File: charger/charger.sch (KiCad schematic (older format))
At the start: 43 parts, among them J1 Barrel_Jack, P1 Digital, P10 CONN_01X01, P11 CONN_01X01, P12 CONN_01X01, P13 CONN_01X01, P2 Power, P3 Analog, P4 Analog, P5 PWM, P6 PWM, P7 Communication, P8 CONN_01X01, P9 CONN_01X01, Q16 2SC1815, Q17 NDP6020, Q18 2SC1815, Q19 NDP6020, Q2 2SC1815, Q20 2SC1815, Q21 NDP6020, Q4 NDP6020, Q5 NDP6020, Q6 NDP6020, Q7 NDP6020, Q8 NDP6020, U1 tp4056charger, U2 tp4056charger, U3 tp4056charger, U4 tp4056charger

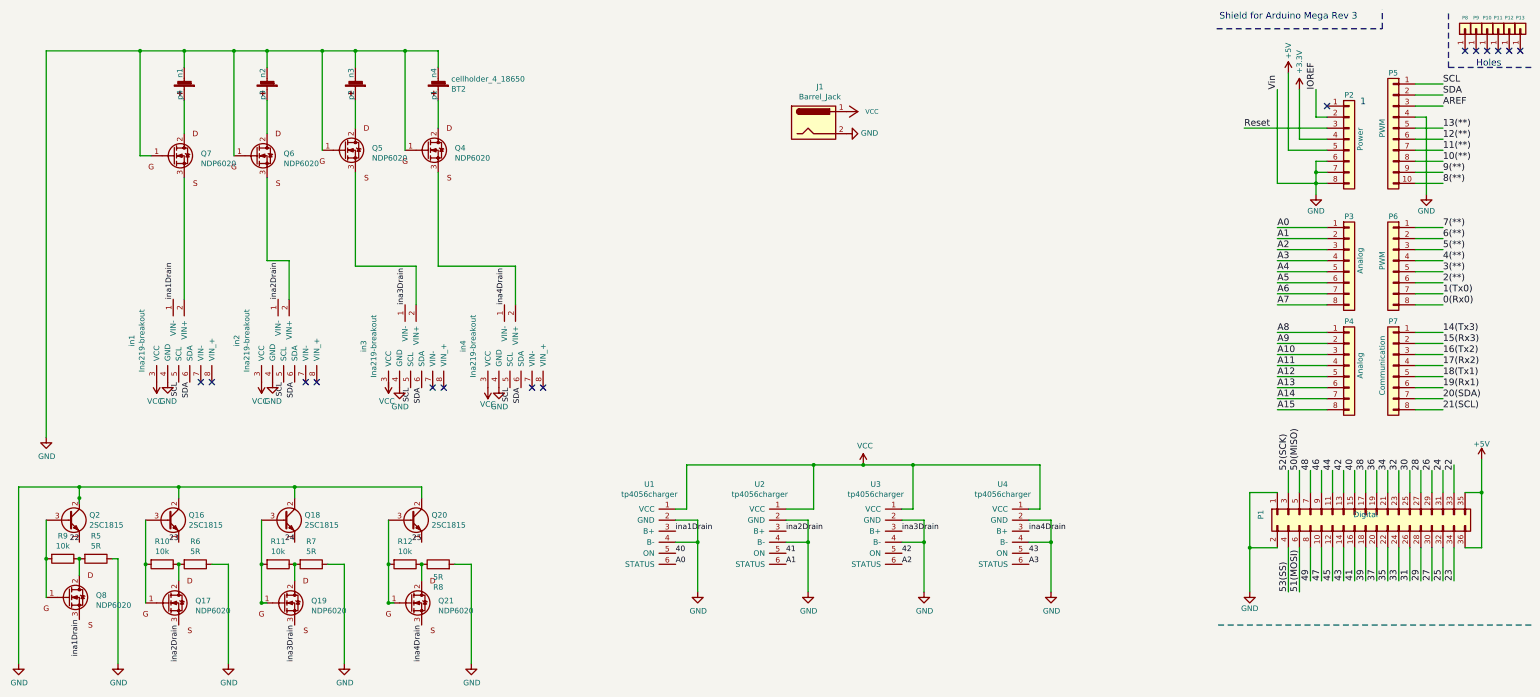
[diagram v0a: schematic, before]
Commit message: adding 2 layer layout, circuit design for 1 and 2 layer
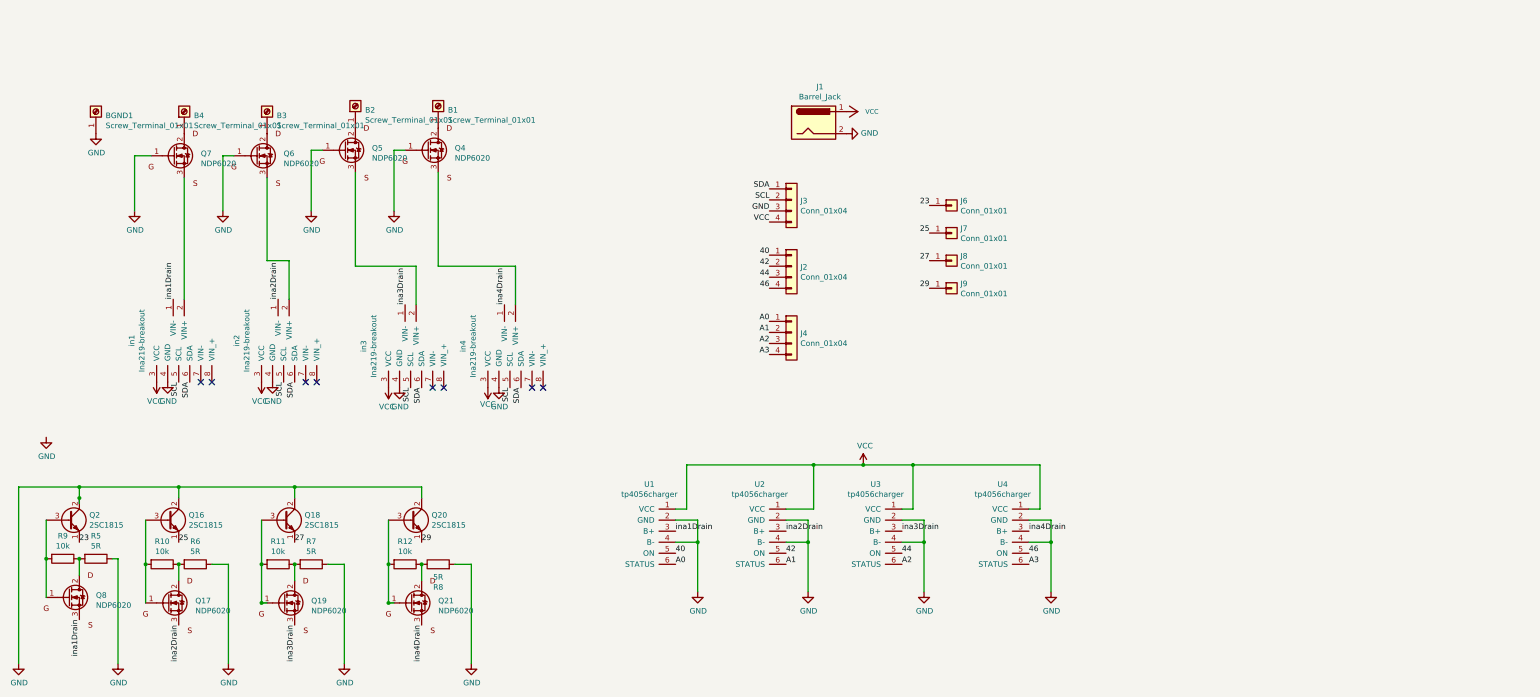
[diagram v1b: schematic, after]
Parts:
- removed BT2: cellholder_4_18650, charger:battery_holder, symbol charger-rescue:cellholder_4_18650-batteryholder1
- removed P1: Digital, Socket_Arduino_Mega:Socket_Strip_Arduino_2x18, symbol Connector_Generic:Conn_02x18_Odd_Even
- removed P10, P11, P12, P13, P8, P9: CONN_01X01, Socket_Arduino_Mega:Arduino_1pin, symbol Connector_Generic:Conn_01x01
- removed P2: Power, Socket_Arduino_Mega:Socket_Strip_Arduino_1x08, symbol Connector_Generic:Conn_01x08
- removed P3, P4: Analog, Socket_Arduino_Mega:Socket_Strip_Arduino_1x08, symbol Connector_Generic:Conn_01x08
- removed P5: PWM, Socket_Arduino_Mega:Socket_Strip_Arduino_1x10, symbol Connector_Generic:Conn_01x10
- removed P6: PWM, Socket_Arduino_Mega:Socket_Strip_Arduino_1x08, symbol Connector_Generic:Conn_01x08
- removed P7: Communication, Socket_Arduino_Mega:Socket_Strip_Arduino_1x08, symbol Connector_Generic:Conn_01x08
- added B1, B2, B3, B4, BGND1: Screw_Terminal_01x01, MountingHole:MountingHole_2.2mm_M2_DIN965_Pad, symbol Connector:Screw_Terminal_01x01
- added J2, J3, J4: Conn_01x04, Connector_PinHeader_2.54mm:PinHeader_1x04_P2.54mm_Vertical, symbol Connector_Generic:Conn_01x04
- added J6, J7, J8, J9: Conn_01x01, Connector_PinHeader_2.54mm:PinHeader_1x01_P2.54mm_Vertical, symbol Connector_Generic:Conn_01x01
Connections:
- net labels removed: +3.3V, +5V, 0(Rx0), 1(Tx0), 10(**), 11(**), 12(**), 13(**), 14(Tx3), 15(Rx3), 16(Tx2), 17(Rx2), 18(Tx1), 19(Rx1), 2(**), 20(SDA), 21(SCL), 22, 24, 26, 28, 3(**), 30, 31, 32, 33, 34, 35, 36, 37, 38, 39, 4(**), 41, 43, 45, 47, 48, 49, 5(**), 50(MISO), 51(MOSI), 52(SCK), 53(SS), 6(**), 7(**), 8(**), 9(**), A10, A11, A12, A13, A14, A15, A4, A5, A6, A7, A8, A9, AREF, IOREF, Reset, Vin
- wire segments 190 -> 78
- no-connect marks 15 -> 8
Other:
- note removed: "1"
- note removed: "Holes"
- note removed: "Shield for Arduino Mega Rev 3"
